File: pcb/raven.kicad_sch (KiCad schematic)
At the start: 10 parts, among them J1 Conn_02x20_Odd_Even, J2 Conn_01x04_MountingPin, J3 Screw_Terminal_01x02, J4 Screw_Terminal_01x02

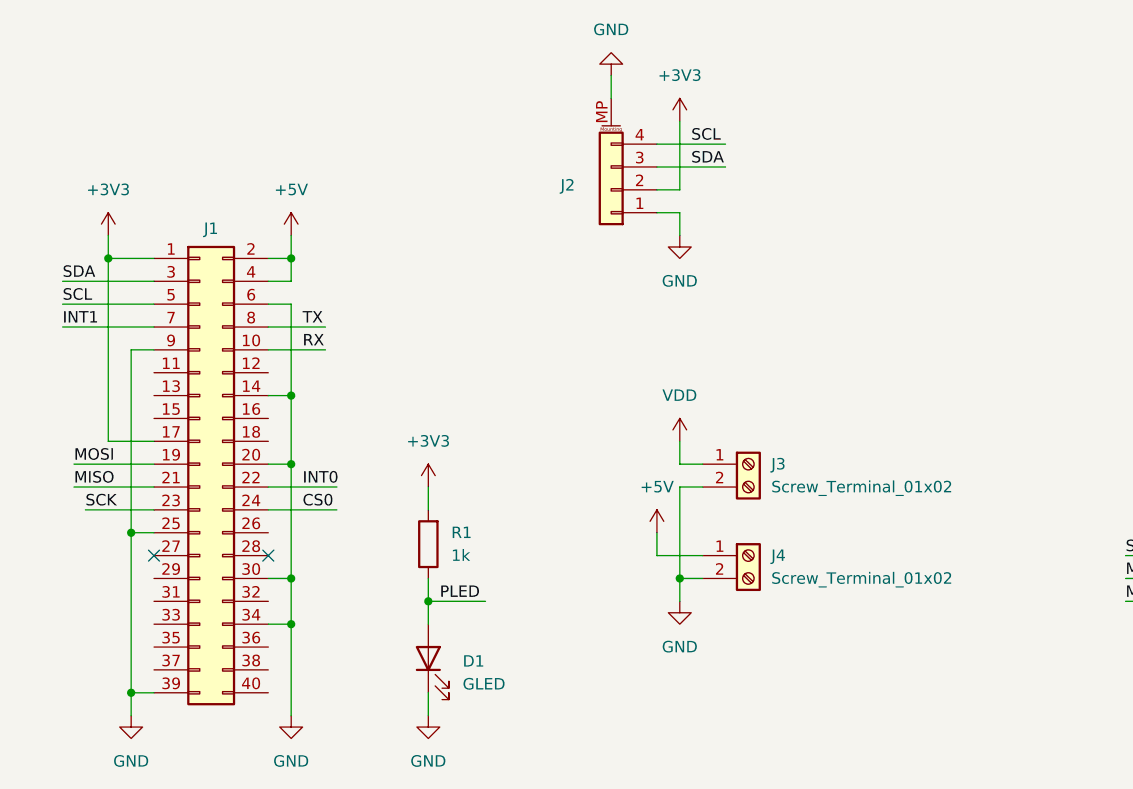
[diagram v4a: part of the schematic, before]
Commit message: Add another qwic connector
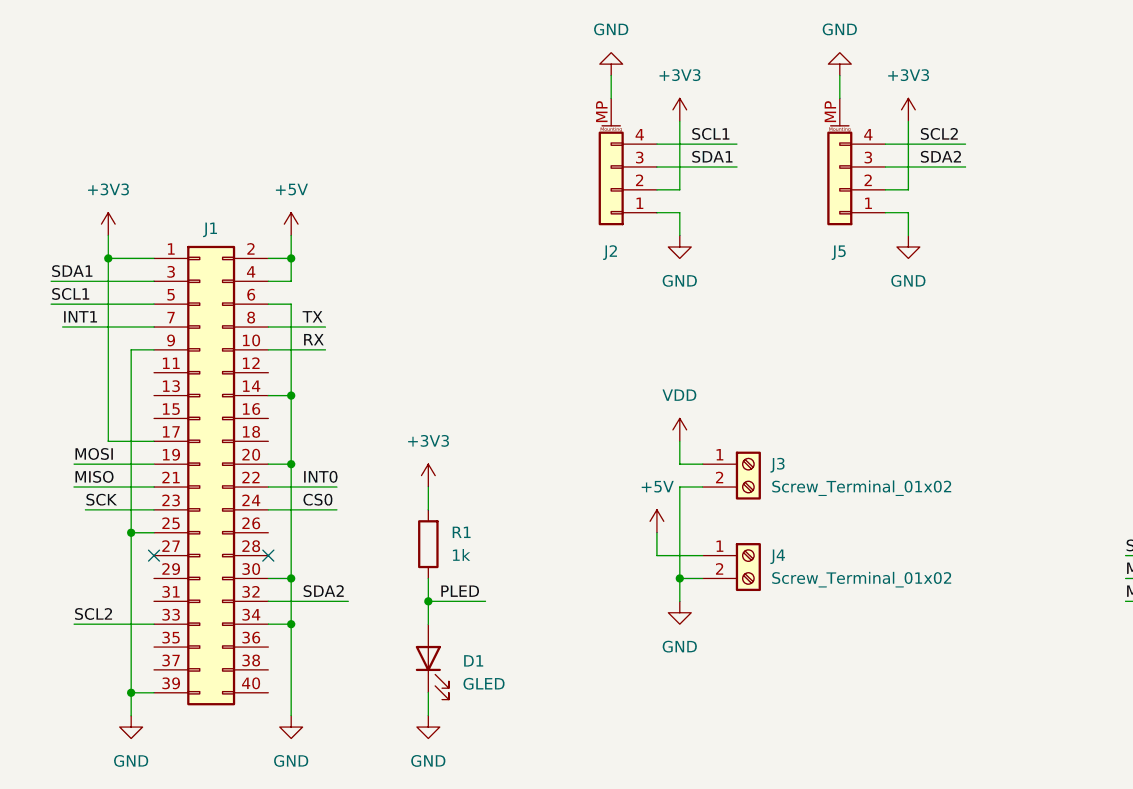
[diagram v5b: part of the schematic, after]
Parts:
- added J5: Conn_01x04_MountingPin, Connector_JST:JST_SH_SM04B-SRSS-TB_1x04-1MP_P1.00mm_Horizontal, symbol Connector_Generic_MountingPin:Conn_01x04_MountingPin
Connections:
- net +3V3: now also J5.2 (Pin_2)
- net GND: now also J5.1 (Pin_1), J5.MP (MountPin)
- net SCL: no longer J1.5 (Pin_5), J2.4 (Pin_4)
- net SDA: no longer J1.3 (Pin_3), J2.3 (Pin_3)
- net SDA2: now reaches J1.32 (Pin_32)
- net SDA2: now also J5.3 (Pin_3)
- net SCL2: now reaches J1.33 (Pin_33)
- net SCL2: now also J5.4 (Pin_4)
- new net SCL1: J1.5 (Pin_5), J2.4 (Pin_4)
- new net SDA1: J1.3 (Pin_3), J2.3 (Pin_3)

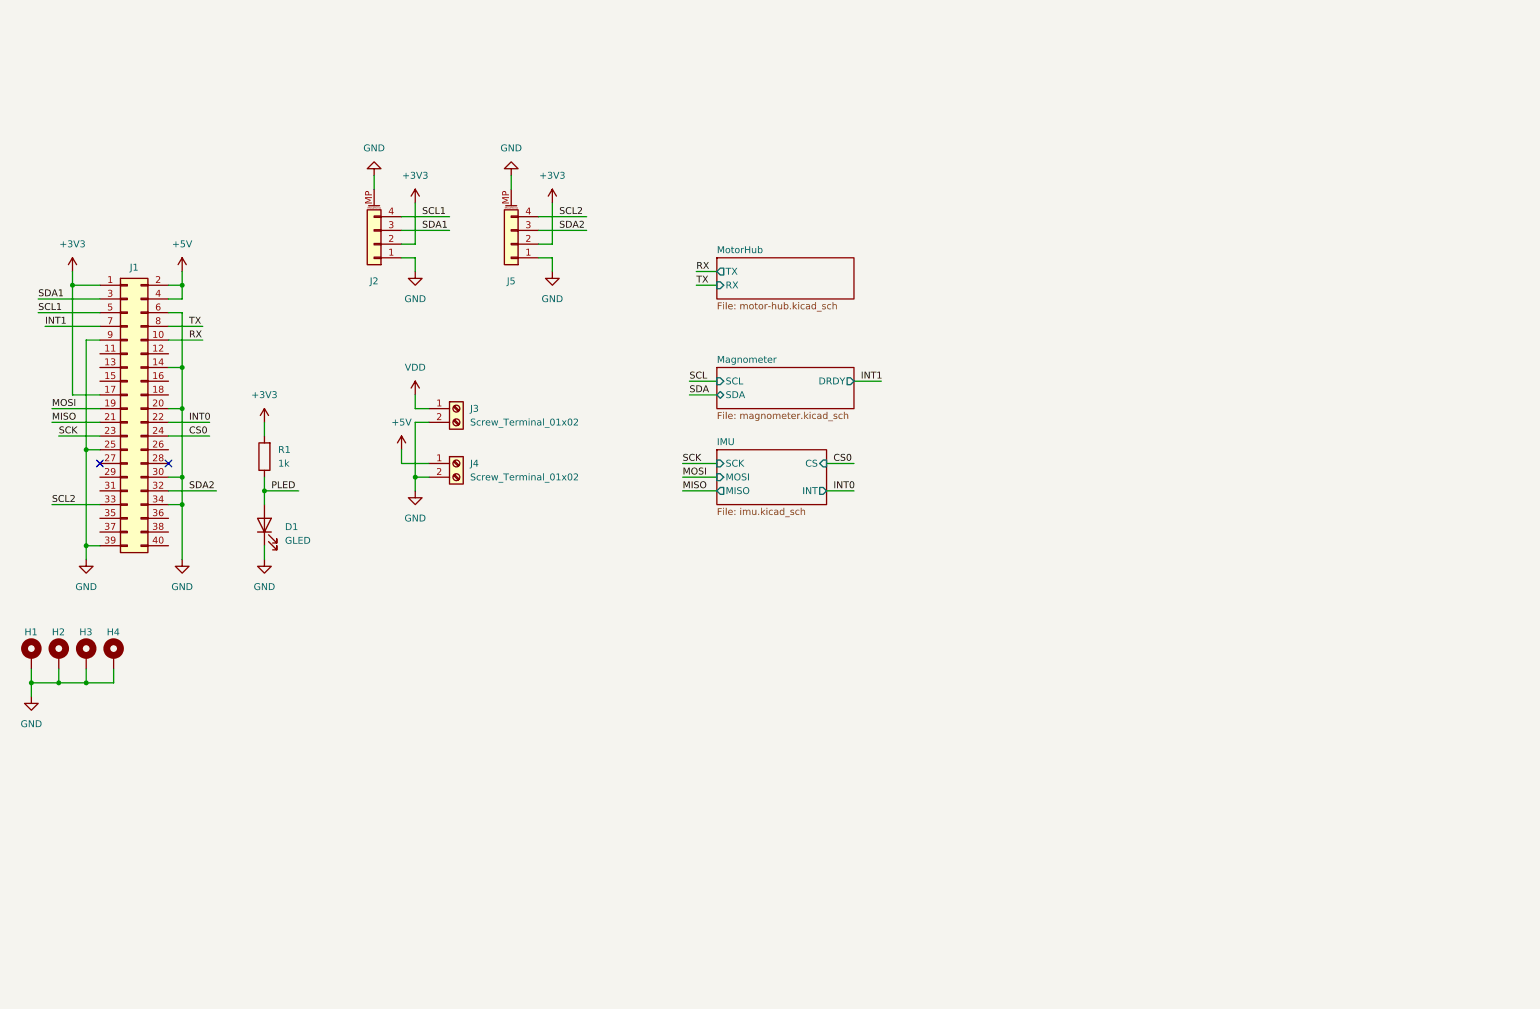
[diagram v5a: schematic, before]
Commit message: Finish first draft schematic
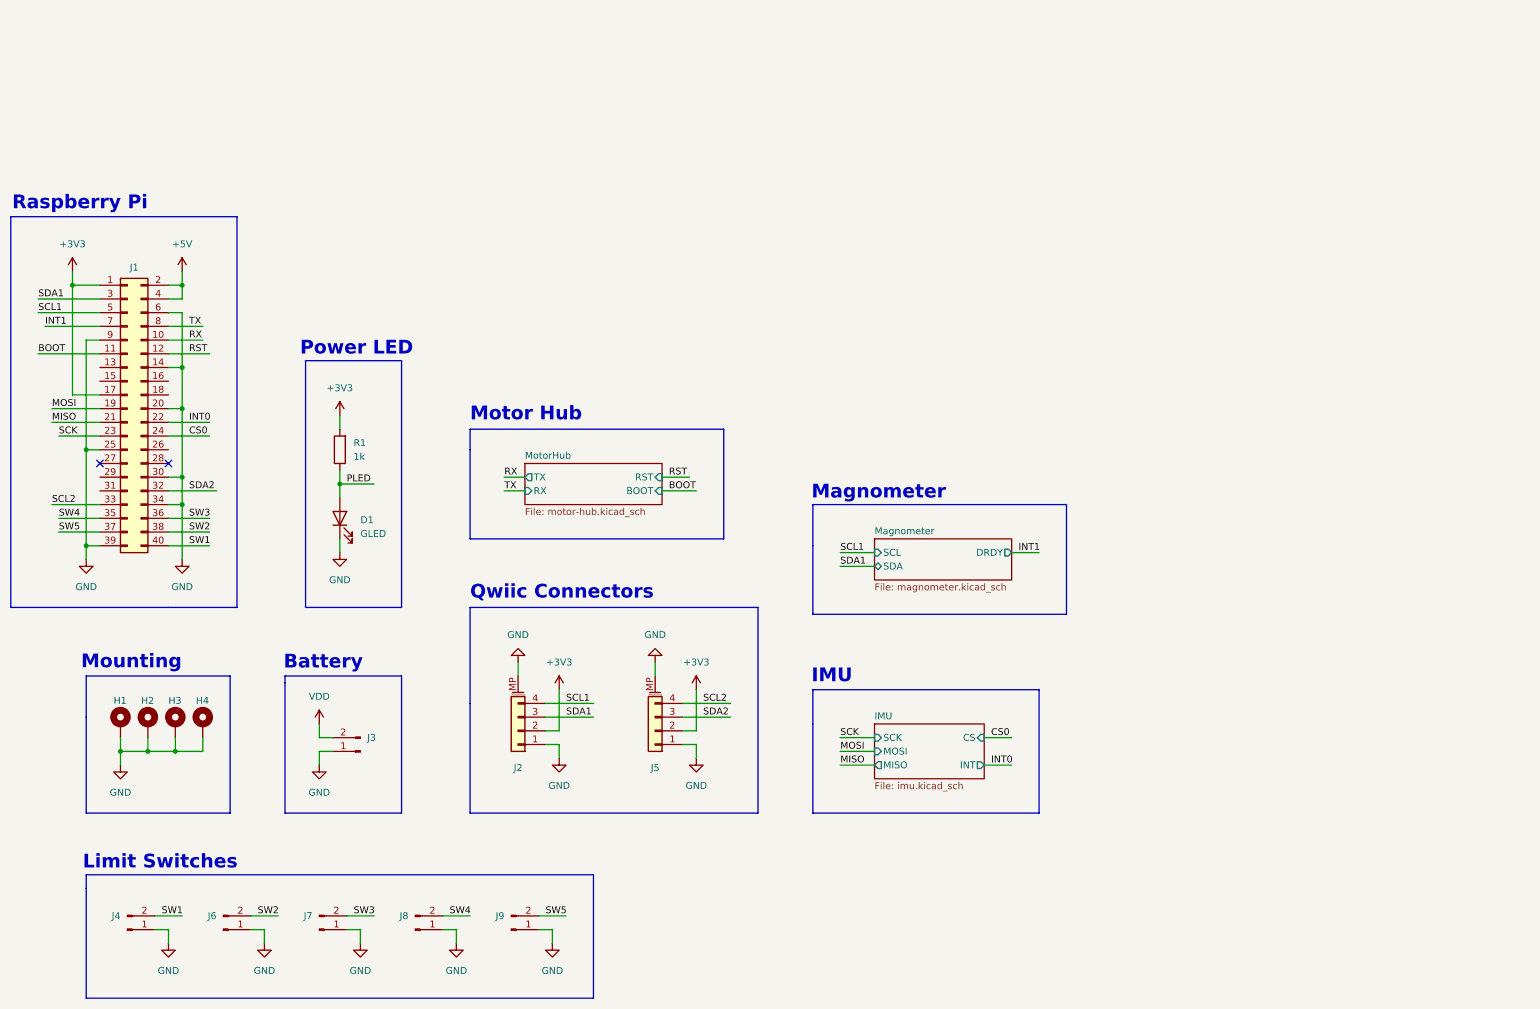
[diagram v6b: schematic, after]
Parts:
- removed J3, J4: Screw_Terminal_01x02, TerminalBlock_Phoenix:TerminalBlock_Phoenix_MKDS-1,5-2_1x02_P5.00mm_Horizontal, symbol Connector:Screw_Terminal_01x02
- added J3: Conn_01x02_Pin, Connector_AMASS:AMASS_XT30PW-M_1x02_P2.50mm_Horizontal, symbol Connector:Conn_01x02_Pin
- added J4, J6, J7, J8, J9: Conn_01x02_Pin, Connector_PinHeader_2.54mm:PinHeader_1x02_P2.54mm_Vertical, symbol Connector:Conn_01x02_Pin
- J1: footprint Connector_PinSocket_2.54mm:PinSocket_2x20_P2.54mm_Vertical -> Connector_PinHeader_2.54mm:PinHeader_2x20_P2.54mm_Vertical; LCSC C7499354 -> (none)
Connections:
- net GND: now also J3.1 (Pin_1), J4.1 (Pin_1), J6.1 (Pin_1), J7.1 (Pin_1), J8.1 (Pin_1), J9.1 (Pin_1)
- net VDD: now also J3.2 (Pin_2)
- net BOOT: now reaches J1.11 (Pin_11)
- net RST: now reaches J1.12 (Pin_12)
- net SW4: now reaches J1.35 (Pin_35)
- net SW4: now also J8.2 (Pin_2)
- net SW3: now reaches J1.36 (Pin_36)
- net SW3: now also J7.2 (Pin_2)
- net SW5: now reaches J1.37 (Pin_37)
- net SW5: now also J9.2 (Pin_2)
- net SW2: now reaches J1.38 (Pin_38)
- net SW2: now also J6.2 (Pin_2)
- net SW1: now reaches J1.40 (Pin_40)
- net SW1: now also J4.2 (Pin_2)
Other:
- sheet MotorHub ports: added BOOT, RST; removed none
- note added: "Battery"
- note added: "IMU"
- note added: "Limit Switches"
- note added: "Magnometer"
- note added: "Motor Hub"
- note added: "Mounting"
- note added: "Power LED"
- note added: "Qwiic Connectors"
- note added: "Raspberry Pi"
- moved on the sheet: D1, H1, H2, H3, H4, J2, J5, R1

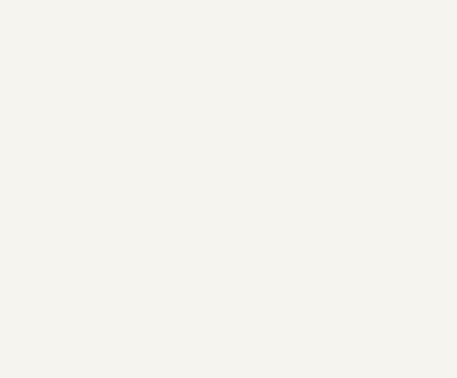
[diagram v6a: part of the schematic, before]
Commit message: Start on regulator
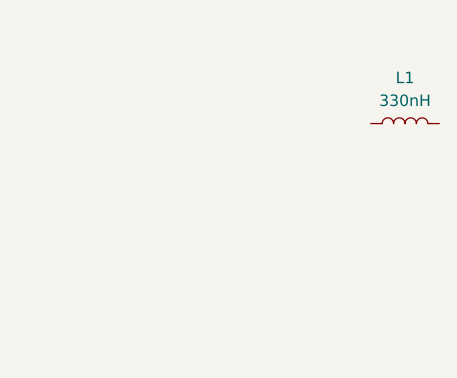
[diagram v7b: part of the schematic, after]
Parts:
- added L1: 330nH, symbol Device:L
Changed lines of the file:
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@@
+		)
+	)
+	(symbol
+		(lib_id "Device:L")
+		(at 213.36 41.91 90)
+		(unit 1)
+		(exclude_from_sim no)
+		(in_bom yes)
+		(on_board yes)
+		(dnp no)
+		(fields_autoplaced yes)
+		(property "Reference" "L1"
+			(at 213.36 36.83 90)
+			(effects
+				(font
+					(size 1.27 1.27)
+				)
+			)
+		)
+		(property "Value" "330nH"
+			(at 213.36 39.37 90)
+			(effects
+				(font
+					(size 1.27 1.27)
+				)
+			)
+		)
+		(property "Footprint" ""
+			(at 213.36 41.91 0)
+			(effects
+				(font
+					(size 1.27 1.27)
+				)
+				(hide yes)
+			)
+		)
+		(property "Datasheet" "~"
+			(at 213.36 41.91 0)
+			(effects
+				(font
+					(size 1.27 1.27)
+				)
+				(hide yes)
+			)
+		)
+		(property "Description" "Inductor"
+			(at 213.36 41.91 0)
+			(effects
+				(font
+					(size 1.27 1.27)
+				)
+				(hide yes)
+			)
+		)
+		(property "LCSC" "C167211"
+			(at 213.36 41.91 90)
+			(effects
+				(font
+					(size 1.27 1.27)
+				)
+				(hide yes)
+			)
+		)
+		(pin "2"
+		)
+		(pin "1"
+		)
+		(instances
+			(project ""
+				(path "/38b0a34b-2047-47f6-90d7-ccdf77e8e212"
+					(reference "L1")
+					(unit 1)
+				)
+			)
 		)
 	)

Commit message: Save progress
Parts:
- added C23: 100n, Capacitor_SMD:C_0603_1608Metric, symbol Device:C
- added C39: 100n, Capacitor_SMD:C_0402_1005Metric, symbol Device:C
- added C40, C41, C42, C43: 47u, Capacitor_SMD:C_1206_3216Metric, symbol Device:C
- added C44: 220n, Capacitor_SMD:C_0603_1608Metric, symbol Device:C
- added C45: 2u2, Capacitor_SMD:C_0805_2012Metric, symbol Device:C
- added C46, C47, C48, C49: 1u, Capacitor_SMD:C_0402_1005Metric, symbol Device:C
- added C50, C51, C52, C53, C54: 22u, Capacitor_SMD:C_0805_2012Metric, symbol Device:C
- added D14: GLED, LED_SMD:LED_0603_1608Metric, symbol Device:LED
- added NT1: SNS, symbol Device:NetTie_2
- added R28, R49, R51, R52, R53, R54: R, Resistor_SMD:R_0402_1005Metric, symbol Device:R
- added R50: 1k, Resistor_SMD:R_0402_1005Metric, symbol Device:R
- added U9: TPS548B28RWWR, Footprints:TPS548B28RWWR, symbol Symbols:TPS548B28RWWR
- L1: footprint (none) -> Inductor_SMD:L_Changjiang_FXL0630
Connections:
- net +5V: now also L1.2, C39.2, C40.1, C41.1, C42.1, C43.1, R50.2, R53.1
- net GND: now also C39.1, C40.2, C41.2, C42.2, C43.2, C45.1, C46.2, C47.2, C48.2, C49.2, C50.2, C51.2, C52.2, C53.2, C54.2, NT1.2, R28.2, R49.2, R52.2, U9.11 (PGND), U9.12 (PGND), U9.13 (PGND), U9.14 (PGND), U9.15 (PGND), U9.16 (PGND), U9.17 (PGND), U9.18 (PGND), U9.2 (AGND)
- net VDD: now also C46.1, C47.1, C48.1, C49.1, C50.1, C51.1, C52.1, C53.1, C54.1, R51.1, U9.10 (VIN), U9.21 (VIN)
- net SW: now reaches L1.1
- net SW: now also C23.2, U9.20 (SW)
- net BOOT renamed BT0
- new net: D14.2 (A), R50.1
- new net: C23.1, U9.1 (BOOT)
- new net: C45.2, U9.19 (VCC)
- new net EN: R51.2, R52.1, U9.8 (EN)
- new net FB: R53.2, R54.1, U9.7 (FB)
- new net MODE: R49.1, U9.4 (MODE)
- new net PGOOD: D14.1 (K), U9.9 (GOOD)
- new net SS: C44.1, U9.5 (SS)
- new net TR: R28.1, U9.3 (TRIP)
- new net VSNS: C44.2, NT1.1, R54.2, U9.6 (VSNS)
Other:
- sheet MotorHub ports: added BT0; removed BOOT
- moved on the sheet: L1
